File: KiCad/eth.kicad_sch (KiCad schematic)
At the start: 258 parts, among them J18 RJ45_LED_Shielded_x2, J19 RJE361882415, J20 RJ45_LED_Shielded_x2, U10 H5VU25U, U11 H5VU25U, U12 KTI226V, U13 KTI226V, U14 ZD25Q64BSIGT, U15 ZD25Q64BSIGT, U16 H5VU25U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

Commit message: Connect clkreq to nics, fix pcie x1 footprint
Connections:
- net ETH1.~{CLKREQ}: now reaches U13.3 (PE_CLKREQ_N)
- net ETH3.~{CLKREQ}: now reaches U21.3 (PE_CLKREQ_N)
- net ETH2.~{CLKREQ}: now reaches U20.3 (PE_CLKREQ_N)
- net ETH4.~{CLKREQ}: now reaches U26.3 (PE_CLKREQ_N)
- net ETH0.~{CLKREQ}: now reaches U12.3 (PE_CLKREQ_N)
- no-connect marks 35 -> 30
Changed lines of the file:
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@@
 	)
 	(no_connect
-		(at 54.61 92.71)
-	)
-	(no_connect
 		(at 52.07 226.06)
 	)
 	(no_connect
-		(at 326.39 213.36)
-	)
-	(no_connect
 		(at 326.39 226.06)
 	)
 	(no_connect
-		(at 48.26 347.98)
-	)
-	(no_connect
 		(at 52.07 223.52)
 	)
@@
 	)
 	(no_connect
-		(at 328.93 95.25)
-	)
-	(no_connect
 		(at 326.39 223.52)
 	)
@@
 		(at 328.93 110.49)
 	)
-	(no_connect
-		(at 52.07 210.82)
-	)
 	(bus_entry
 		(at 311.15 62.23)
@@
 	)
 	(bus_entry
+		(at 308.61 210.82)
+		(size 2.54 2.54)
+		(stroke
+			(width 0)
+			(type default)
+		)
+	)
+	(bus_entry
+		(at 311.15 92.71)
+		(size 2.54 2.54)
+		(stroke
+			(width 0)
+			(type default)
+		)
+	)
+	(bus_entry
 		(at 311.15 90.17)
 		(size 2.54 2.54)
@@
 	)
 	(bus_entry
+		(at 36.83 90.17)
+		(size 2.54 2.54)
+		(stroke
+			(width 0)
+			(type default)
+		)
+	)
+	(bus_entry
 		(at 308.61 205.74)
 		(size 2.54 2.54)
@@
 	)
 	(bus_entry
+		(at 30.48 345.44)
+		(size 2.54 2.54)
+		(stroke
+			(width 0)
+			(type default)
+		)
+	)
+	(bus_entry
+		(at 34.29 208.28)
+		(size 2.54 2.54)
+		(stroke
+			(width 0)
+			(type default)
+		)
+	)
+	(bus_entry
 		(at 30.48 325.12)
 		(size 2.54 2.54)
@@
 	(wire
 		(pts
+			(xy 311.15 213.36) (xy 326.39 213.36)
+		)
+		(stroke
+			(width 0)
+			(type default)
+		)
+	)
+	(wire
+		(pts
 			(xy 33.02 327.66) (xy 48.26 327.66)
 		)
@@
 	(wire
 		(pts
+			(xy 39.37 92.71) (xy 54.61 92.71)
+		)
+		(stroke
+			(width 0)
+			(type default)
+		)
+	)
+	(wire
+		(pts
 			(xy 518.16 203.2) (xy 519.43 203.2)
 		)
@@
 	(wire
 		(pts
+			(xy 36.83 210.82) (xy 52.07 210.82)
+		)
+		(stroke
+			(width 0)
+			(type default)
+		)
+	)
+	(wire
+		(pts
 			(xy 394.97 190.5) (xy 394.97 199.39)
 		)
@@
 		)
 	)
+	(bus
+		(pts
+			(xy 311.15 90.17) (xy 311.15 92.71)
+		)
+		(stroke
+			(width 0)
+			(type default)
+		)
+	)
 	(wire
 		(pts
@@
 		)
 	)
+	(bus
+		(pts
+			(xy 36.83 87.63) (xy 36.83 90.17)
+		)
+		(stroke
+			(width 0)
+			(type default)
+		)
+	)
 	(wire
 		(pts
@@
 		)
 	)
+	(bus
+		(pts
+			(xy 30.48 342.9) (xy 30.48 345.44)
+		)
+		(stroke
+			(width 0)
+			(type default)
+		)
+	)
 	(wire
 		(pts
@@
 	(wire
 		(pts
+			(xy 33.02 347.98) (xy 48.26 347.98)
+		)
+		(stroke
+			(width 0)
+			(type default)
+		)
+	)
+	(wire
+		(pts
 			(xy 139.7 168.91) (xy 139.7 170.18)
 		)
@@
 		)
 	)
+	(bus
+		(pts
+			(xy 308.61 208.28) (xy 308.61 210.82)
+		)
+		(stroke
+			(width 0)
+			(type default)
+		)
+	)
 	(wire
 		(pts
@@
 	(wire
 		(pts
+			(xy 313.69 95.25) (xy 328.93 95.25)
+		)
+		(stroke
+			(width 0)
+			(type default)
+		)
+	)
+	(wire
+		(pts
 			(xy 398.78 69.85) (xy 398.78 76.2)
 		)
@@
 		)
 	)
+	(bus
+		(pts
+			(xy 34.29 205.74) (xy 34.29 208.28)
+		)
+		(stroke
+			(width 0)
+			(type default)
+		)
+	)
 	(wire
 		(pts
@@
 		)
 	)
+	(label "ETH2.~{CLKREQ}"
+		(at 36.83 210.82 0)
+		(effects
+			(font
+				(size 1.27 1.27)
+			)
+			(justify left bottom)
+		)
+	)
 	(label "ETH4.SMBCLK"
 		(at 33.02 317.5 0)
@@
 		)
 	)
+	(label "ETH1.~{CLKREQ}"
+		(at 313.69 95.25 0)
+		(effects
+			(font
+				(size 1.27 1.27)
+			)
+			(justify left bottom)
+		)
+	)
 	(label "ETH1.REFCLK-"
 		(at 313.69 85.09 0)
@@
 		)
 	)
+	(label "ETH3.~{CLKREQ}"
+		(at 311.15 213.36 0)
+		(effects
+			(font
+				(size 1.27 1.27)
+			)
+			(justify left bottom)
+		)
+	)
 	(label "ETH1.Rx0-"
 		(at 313.69 80.01 0)
@@
 			)
 			(justify left bottom)
+		)
+	)
+	(label "ETH0.~{CLKREQ}"
+		(at 39.37 92.71 0)
+		(effects
+			(font
+				(size 1.27 1.27)
+			)
+			(justify left bottom)
+		)
+	)
+	(label "ETH4.~{CLKREQ}"
+		(at 33.02 347.98 0)
+		(effects
+			(font
+				(size 1.27 1.27)
+			)
+			(justify left bottom)

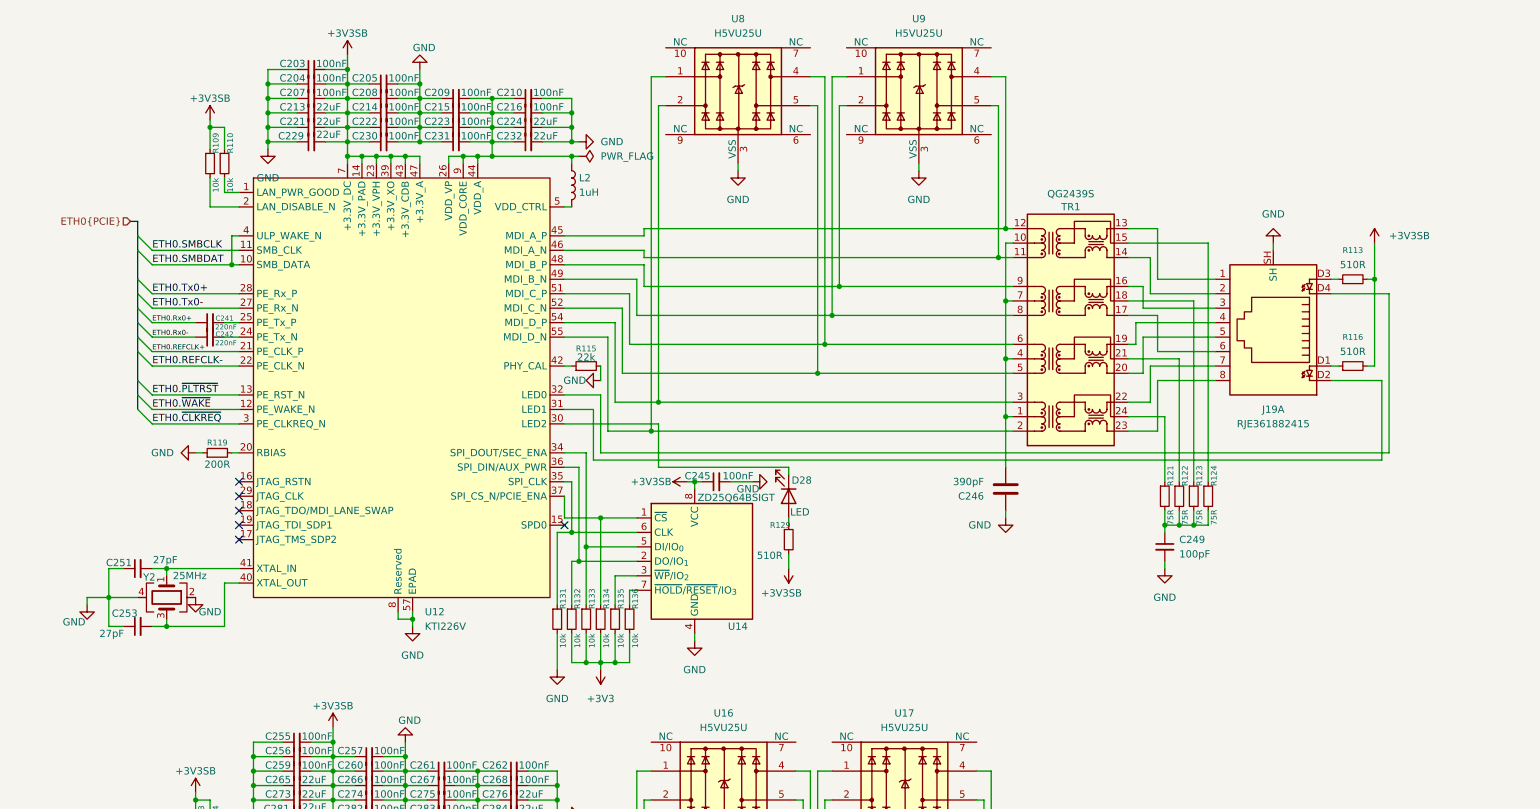
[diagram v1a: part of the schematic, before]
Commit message: Add Ethernet to module sheet
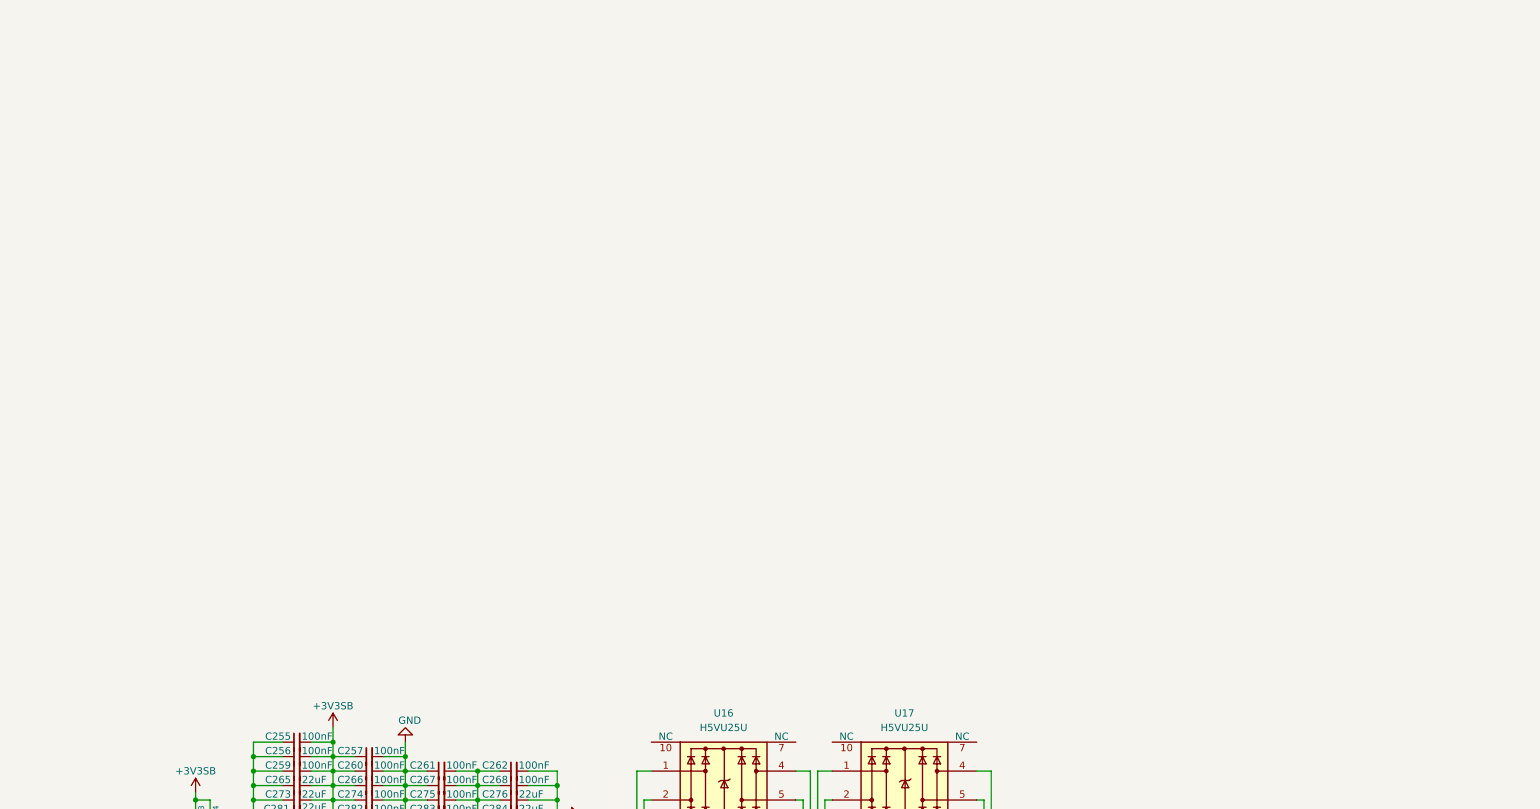
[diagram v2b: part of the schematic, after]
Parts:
- removed C203, C204, C205, C207, C208, C209, C210, C214, C215, C216, C222, C223, C230, C231, C245: 100nF, Capacitor_SMD:C_0402_1005Metric, symbol Device:C_Small
- removed C213, C221, C224, C229, C232: 22uF, Capacitor_SMD:C_0603_1608Metric, symbol Device:C_Small
- removed C241, C242: 220nF, Capacitor_SMD:C_0402_1005Metric, symbol Device:C_Small
- removed C246: 390pF, Capacitor_SMD:C_0402_1005Metric, symbol Device:C
- removed C249: 100pF, Capacitor_SMD:C_0402_1005Metric, symbol Device:C_Small
- removed C251, C253: 27pF, Capacitor_SMD:C_0402_1005Metric, symbol Device:C_Small
- removed D28: LED, LED_SMD:LED_0603_1608Metric, symbol Device:LED
- removed J19: RJE361882415, RJE361882145:AMPHENOL_RJE361882415, symbol Custom:1xRJ45+2xUSB3
- removed L2: 1uH, Inductor_SMD:L_0805_2012Metric, symbol Device:L
- removed R109, R110, R131, R132, R133, R134, R135, R136: 10k, Resistor_SMD:R_0402_1005Metric, symbol Device:R_Small
- removed R113, R116, R129: 510R, Resistor_SMD:R_0402_1005Metric, symbol Device:R_Small
- removed R115: 22k, Resistor_SMD:R_0402_1005Metric, symbol Device:R_Small
- removed R119: 200R, Resistor_SMD:R_0402_1005Metric, symbol Device:R_Small
- removed R121, R122, R123, R124: 75R, Resistor_SMD:R_0402_1005Metric, symbol Device:R_Small
- removed TR1: QG2439S, Custom:QG2439S, symbol Transformer:30F-51NL
- removed U12: KTI226V, Package_DFN_QFN:QFN-56-1EP_7x7mm_P0.4mm_EP5.6x5.6mm_ThermalVias, symbol Custom:KTI226V
- removed U14: ZD25Q64BSIGT, Package_SO:SOIC-8_5.3x5.3mm_P1.27mm, symbol Memory_Flash:W25Q128JVS
- removed U8, U9: H5VU25U, Package_DFN_QFN:Diodes_UDFN-10_1.0x2.5mm_P0.5mm, symbol Power_Protection:D3V3XA4B10LP
- removed Y2: 25MHz, Crystal:Crystal_SMD_3225-4Pin_3.2x2.5mm, symbol Device:Crystal_GND24
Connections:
- no-connect marks 30 -> 24
